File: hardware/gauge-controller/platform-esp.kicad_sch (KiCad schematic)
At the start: 106 parts, among them J1 Conn_ARM_JTAG_SWD_10, J3 PWR_CAN, J4 USB4120-03-C_REVA, J6 TC2030-IDC, SW1 SW_Push, SW2 SW_Push, U1 W25Q128JVS, U2 ESP-PSRAM32, U3 ESP32-S3R2, U4 AP64200Q, U5 LTC2875-DD, Y1 40MHZ

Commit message: Multi gauge pcb design
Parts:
- removed C13: C_Small, Capacitor_SMD:C_0402_1005Metric, symbol Device:C_Small
- removed C23: 10uf, Capacitor_SMD:C_0805_2012Metric_Pad1.18x1.45mm_HandSolder, symbol Device:C_Small
- removed C24: 5.6nf, Capacitor_SMD:C_1206_3216Metric, symbol Device:C_Small
- removed C25: 0.1uf, Capacitor_SMD:C_0805_2012Metric_Pad1.18x1.45mm_HandSolder, symbol Device:C_Small
- removed C26, C27, C28, C29: DNP, Capacitor_SMD:C_0805_2012Metric_Pad1.18x1.45mm_HandSolder, symbol Device:C_Small
- removed C32: 10uF, Capacitor_SMD:C_0402_1005Metric, symbol Device:C_Small
- removed C33, C34, C35, C36, C37, C38, C39, C40, C41: 1uF, Capacitor_SMD:C_0402_1005Metric, symbol Device:C_Small
- removed C9: 0.1uF, Capacitor_SMD:C_0402_1005Metric, symbol Device:C_Small
- removed D1, D10, D11, D2, D3, D4, D5, D8, D9: WS2812B, LED_SMD:LED_WS2812B_PLCC4_5.0x5.0mm_P3.2mm, symbol LED:WS2812B
- removed J1: Conn_ARM_JTAG_SWD_10, Connector:Tag-Connect_TC2050-IDC-NL_2x05_P1.27mm_Vertical, symbol Connector:Conn_ARM_JTAG_SWD_10
- removed J6: TC2030-IDC, Connector:Tag-Connect_TC2030-IDC-NL_2x03_P1.27mm_Vertical, symbol Connector_TDC:TC2030-IDC
- removed L4: 6.8uh, Inductor_SMD:L_Bourns-SRN6028, symbol Device:L_Small
- removed R23: 52.3k, Resistor_SMD:R_0603_1608Metric_Pad0.98x0.95mm_HandSolder, symbol Device:R_Small
- removed R24: 10k, Resistor_SMD:R_0603_1608Metric_Pad0.98x0.95mm_HandSolder, symbol Device:R_Small
- removed R29: 0, Resistor_SMD:R_0402_1005Metric, symbol Device:R_Small
- removed R3: 100k, Resistor_SMD:R_0402_1005Metric, symbol Device:R_Small
- removed R4: 442k, Resistor_SMD:R_0402_1005Metric, symbol Device:R_Small
- removed TP1, TP2: 3V3OUT, TestPoint:TestPoint_Pad_D1.0mm, symbol Connector:TestPoint
- removed TP12: BL, TestPoint:TestPoint_Pad_D1.0mm, symbol Connector:TestPoint
- removed TP13: VDD3V3, TestPoint:TestPoint_Pad_D1.0mm, symbol Connector:TestPoint
- removed TP14: GND, TestPoint:TestPoint_Pad_D1.0mm, symbol Connector:TestPoint
- removed TP5: NEO_OUT, TestPoint:TestPoint_Pad_D1.0mm, symbol Connector:TestPoint
- removed U2: ESP-PSRAM32, Package_SO:SOIC-8_3.9x4.9mm_P1.27mm, symbol Memory_RAM:ESP-PSRAM32
- removed U4: AP64200Q, Package_SO:SOIC-8-1EP_3.9x4.9mm_P1.27mm_EP2.29x3mm_ThermalVias, symbol AP1509-50SG-13:AP64200Q
- added C19: 0.1uF, Capacitor_SMD:C_0402_1005Metric, symbol Device:C_Small
- added C20: 0.1uF, Capacitor_SMD:C_0805_2012Metric, symbol Device:C_Small
- added C21: 22uF, Capacitor_SMD:C_0805_2012Metric, symbol Device:C_Small
- added D11: D_Small, Diode_SMD:D_SOD-123F, symbol Device:D_Small
- added J4: Conn_01x12, ConeCodes:GC9A01_disp, symbol Connector_Generic:Conn_01x12
- added Q1: Q_NPN_EBC, Package_TO_SOT_SMD:TSOT-23, symbol Device:Q_NPN_EBC
- added R18: 10k, Resistor_SMD:R_0402_1005Metric, symbol Device:R_Small
- added R19: 100k, Resistor_SMD:R_0603_1608Metric, symbol Device:R_Small
- added R20: 31k6, Resistor_SMD:R_0603_1608Metric, symbol Device:R_Small
- added R26: 10R, Resistor_SMD:R_0402_1005Metric, symbol Device:R_Small
- added R27: 100k, Resistor_SMD:R_0402_1005Metric, symbol Device:R_Small
- added TP3: MTCK, TestPoint:TestPoint_Pad_D1.0mm, symbol Connector:TestPoint
- added TP4: MTMS, TestPoint:TestPoint_Pad_D1.0mm, symbol Connector:TestPoint
- added U5: ADP2303ARDZ-3.3, Package_SO:SOIC-8-1EP_3.9x4.9mm_P1.27mm_EP2.29x3mm_ThermalVias, symbol Regulator_Switching:ADP2303ARDZ-3.3
- C10: value 1uF -> 10uF; footprint Capacitor_SMD:C_0402_1005Metric -> Capacitor_SMD:C_0805_2012Metric; VOLTAGE (none) -> 25V
- C22: value 10uf -> 22uF; footprint Capacitor_SMD:C_0805_2012Metric_Pad1.18x1.45mm_HandSolder -> Capacitor_SMD:C_0805_2012Metric; DESCRIPTION CAP CER 10UF 25V X5R 0805 -> (none); MPN C0805C106M3PAC7800 -> (none)
- J1: renamed from J4; footprint Connector_GCT_USB:GCT_USB4120-03-C_REVA -> ConeCodes:GCT_USB4120-03-C_REVA; symbol Connector_GCT_USB:USB4120-03-C_REVA -> ConeCodes:USB4120-03-C_REVA
- L3: value 0H -> 6.8uh; footprint Inductor_SMD:L_0402_1005Metric -> Inductor_SMD:L_Bourns-SRN6028; DESCRIPTION (none) -> FIXED IND 6.8UH 2.2A 63 MOHM SMD; MPN (none) -> SRN6028-6R8M
- R21: value 200k -> 10k2; footprint Resistor_SMD:R_0603_1608Metric_Pad0.98x0.95mm_HandSolder -> Resistor_SMD:R_0603_1608Metric; DESCRIPTION RES 200K OHM 5% 1/10W 0603 -> (none); MPN RMCF0603JT200K -> (none)
- R22: value 14k -> 10k; footprint Resistor_SMD:R_0603_1608Metric_Pad0.98x0.95mm_HandSolder -> Resistor_SMD:R_0402_1005Metric; DESCRIPTION RES 14K OHM 1% 1/10W 0603 -> (none); MPN RMCF0603FT14K0 -> (none)
- SW1, SW2: footprint SW_RS-032G05A3-SMRT:SW_RS-032G05A3-SMRT -> ConeCodes:SW_RS-032G05A3-SMRT
- TP10: value DC -> 3V3OUT
- TP11: value RST -> 3V3OUT
- TP6: value FSPID -> MTDO
- TP7: value FSPICS1 -> MTDI
- TP8: value FSPIQ -> TXD
- TP9: value FSPICLK -> RXD
- U1: renamed from U3; footprint Package_DFN_QFN:QFN-56-1EP_7x7mm_P0.4mm_EP5.6x5.6mm -> ConeCodes:QFN-56; symbol MCU_ESP:ESP32-S3R2 -> ConeCodes:ESP32-S3R2; MP ESP32-S3R2 -> (none); MPN (none) -> ESP32-S3
- U3: renamed from U1; footprint Package_SO:SOIC-8_5.23x5.23mm_P1.27mm -> Package_SO:SOIC-8W_5.3x5.3mm_P1.27mm; JLCPCB (none) -> C97521
- Y1: footprint Crystal:Crystal_SMD_2016-4Pin_2.0x1.6mm -> Crystal:Crystal_SMD_3225-4Pin_3.2x2.5mm; JLCPCB (none) -> C9010; MPN ECS-400-10-37B2-CKY-TR -> (none)
- renumbered C17 to C1, C14 to C11, C15 to C12, C16 to C13, C2 to C14, C6 to C15, C30 to C16, C1 to C17, C21 to C18, C19 to C2, C42 to C28, C4 to C3, C5 to C4, C8 to C5, C18 to C6, C20 to C7, C11 to C8, C12 to C9, D6 to D1, J3 to J2, R5 to R1, R12 to R10, R13 to R11, R27 to R12, R16 to R13, R25 to R14, R17 to R15, R26 to R16, R18 to R17, R7 to R2, R20 to R23, R19 to R24, R6 to R3, R14 to R4, R15 to R5, R9 to R6, R10 to R7, R1 to R8, R11 to R9, TP4 to TP1, TP3 to TP2, U5 to U2
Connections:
- net GPIO11 is gone; now on net FSPICS0: U1.16 (GPIO11)
- net VDDCPU is gone; now on net +3V3: C9.1, U1.46 (VDD3P3_CPU)
- net VDDRTC is gone; now on net +3V3: C8.1, U1.20 (VDD3P3_RTC)
- net +3V3: now also C22.1, R22.2, TP11.1, U1.2 (VDD3P3), U1.3 (VDD3P3), C19.2, C21.1, J4.3 (Pin_3), J4.4 (Pin_4), R20.1, R27.1
- net BL: now also R18.1
- net CAN_DRV_N: now also J2.2 (Pin_2); no longer J2.3 (Pin_3)
- net CAN_DRV_P: now also J2.1 (Pin_1); no longer J2.4 (Pin_4)
- net CHIP_PU: now also C19.1
- net DC: now also J4.7 (Pin_7); no longer TP10.1
- net EXT_VIN: now also J2.4 (Pin_4); no longer J2.2 (Pin_2)
- net FSPICLK: now also J4.9 (Pin_9); no longer TP9.1
- net FSPICS0: now also J4.8 (Pin_8), R27.2; no longer U1.39 (GPIO34)
- net FSPID: no longer TP6.1
- net FSPIQ: now also J4.10 (Pin_10); no longer TP8.1
- net GND: now also C10.1, C22.2, J2.3 (Pin_3), TP10.1, C21.2, J4.1 (Pin_1), J4.12 (Pin_12), J4.5 (Pin_5), J4.6 (Pin_6), Q1.1 (E), U5.7 (GND), U5.9 (PADGND); no longer C10.2, C22.1, J2.1 (Pin_1)
- net GPIO10: now also R14.2, R16.1, TP2.1
- net GPIO2: no longer R14.2, R16.1, TP2.1
- net GPIO6: no longer TP11.1
- net MTCK: now also TP3.1
- net MTDI: now also TP7.1
- net MTDO: now also TP6.1
- net MTMS: now also TP4.1
- net U0RXD: now also TP9.1
- net U0TXD: now also TP8.1
- net USB_VBUS: now also D11.2 (A)
- net VIN: now also C10.2, D11.1 (K), R19.1, U5.2 (Vin), U5.3 (EN); no longer C22.2
- net MCU_SPIWP: now reaches R7.2, U1.31 (SPIWP)
- net MCU_SPIHD: now reaches R6.2, U1.30 (SPIHD)
- net FB: now reaches R21.1
- net FB: now also R20.2, U5.5 (FB)
- net LCD_BL_DIV: now reaches R22.1
- net LCD_BL_DIV: now also Q1.2 (B), R18.2
- net MCU_SPIQ: now reaches R10.2, U1.34 (SPIQ)
- net MCU_SPICLK: now reaches R9.2, U1.33 (SPICLK)
- net MCU_SPID: now reaches R11.2, U1.35 (SPID)
- net MCU_U0TXD: now reaches R3.2, U1.49 (U0TXD)
- net MCU_XTAL_N: now reaches R2.2, U1.53 (XTAL_N)
- net CHIP_PU_BOOTSTRAP: now reaches C18.1, SW1.2
- net FSPICS1 renamed GPIO9
- net GPIO9: now also J4.11 (Pin_11); no longer TP7.1
- net SPICLK_N: no longer names the net of U1.36 (SPICLK_N)
- net SPICLK_P: no longer names the net of U1.37 (SPICLK_P)
- net SPICLK_P: no longer C10.1
- net SPICS0 renamed MCU_SPICS0
- net SPICS1: no longer names the net of U1.28 (SPICS1)
- removed net VDD3V3: L3.1, U1.2 (VDD3P3), U1.3 (VDD3P3)
- new net BST: C20.1, U5.1 (BST)
- new net GPIO34: U1.39 (GPIO34)
- new net LCD_LEDK: J4.2 (Pin_2), R26.1
- new net PGOOD: R19.2, U5.4 (PGOOD)
- new net Q_LEDK: Q1.3 (C), R26.2
- new net SW: C20.2, L3.1, U5.8 (SW)
- no-connect marks 24 -> 18
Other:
- added sheet neopixels (neopixels.kicad_sch)
- note removed: "0R resistors should be near chip not cpu"
- note removed: "Pretty sure the resistor network here needs to be recalculated for 3.3V. Consult Datasheet"
- moved on the sheet: AE1, C14, C15, C16, C17, C18, C28, C3, C4, C5, C8, C9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

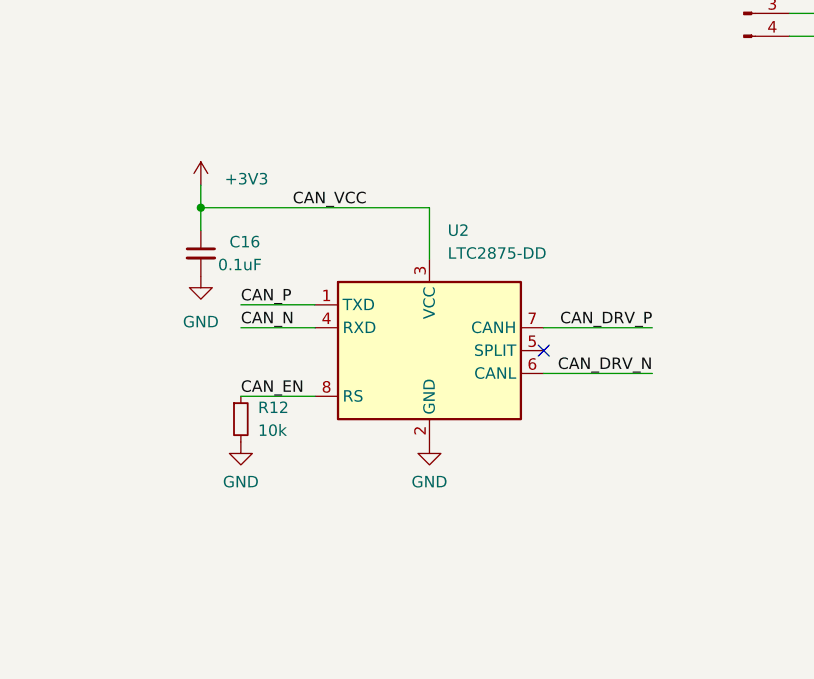
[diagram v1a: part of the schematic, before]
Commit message: Update PCBs to share the same components
* 3x flash memory
* CAN transciever
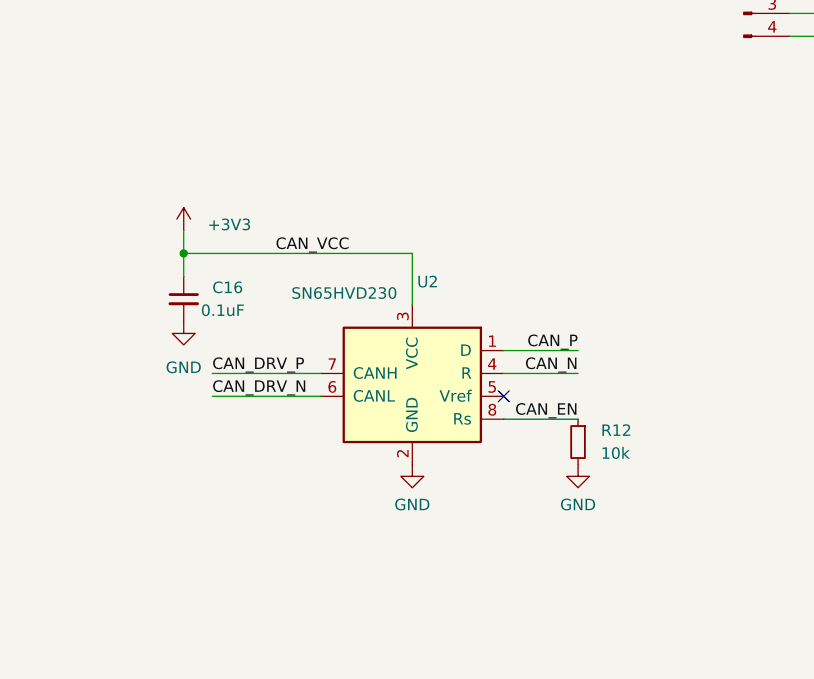
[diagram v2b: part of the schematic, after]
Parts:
- removed U2: LTC2875-DD, Package_DFN_QFN:DFN-8-1EP_3x3mm_P0.5mm_EP1.66x2.38mm, symbol Interface_CAN_LIN:LTC2875-DD
- added U2: SN65HVD230, Package_SO:SOIC-8_3.9x4.9mm_P1.27mm, symbol Interface_CAN_LIN:SN65HVD230
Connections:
- net +3V3: now also U2.3 (VCC)
- net CAN_DRV_N: now also U2.6 (CANL)
- net CAN_DRV_P: now also U2.7 (CANH)
- net CAN_EN: now also U2.8 (Rs)
- net CAN_N: now also U2.4 (R)
- net CAN_P: now also U2.1 (D)
- net GND: now also U2.2 (GND)
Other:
- moved on the sheet: C16
